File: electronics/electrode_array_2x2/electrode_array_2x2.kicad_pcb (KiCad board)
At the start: 2 copper layers, 2 parts

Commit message: WIP PCB layout
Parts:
- added J1: Conn_01x04, Connector_JST:JST_PH_B4B-PH-SM4-TB_1x04-1MP_P2.00mm_Vertical, F.Cu at (150.0, 105.0)
- added J2: Electrode_A1, SquantorSpecial:hugepad_50X15hole, F.Cu at (145.0, 100.0)
- added J3: Electrode_B1, SquantorSpecial:hugepad_50X15hole, F.Cu at (155.0, 100.0)
- added J4: Electrode_A2, SquantorSpecial:hugepad_50X15hole, F.Cu at (145.0, 110.0)
- added J5: Electrode_B2, SquantorSpecial:hugepad_50X15hole, F.Cu at (155.0, 110.0)
- N2: value 20190704 -> 20191222
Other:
- board outline added: 20 x 20 mm
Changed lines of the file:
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@@
-(kicad_pcb (version 20171130) (host pcbnew 5.1.2-f72e74a~84~ubuntu18.04.1)
+(kicad_pcb (version 20171130) (host pcbnew 5.1.5-52549c5~84~ubuntu18.04.1)
   (general
     (thickness 1.6)
-    (drawings 0)
+    (drawings 4)
     (tracks 0)
     (zones 0)
-    (modules 2)
-    (nets 1)
+    (modules 7)
+    (nets 5)
   )
   (page A4)
@@
   )
   (net 0 "")
+  (net 1 /Electrode_B2)
+  (net 2 /Electrode_A2)
+  (net 3 /Electrode_B1)
+  (net 4 /Electrode_A1)
   (net_class Default "This is the default net class."
     (clearance 0.1524)
@@
     (uvia_dia 0.381)
     (uvia_drill 0.254)
+    (add_net /Electrode_A1)
+    (add_net /Electrode_A2)
+    (add_net /Electrode_B1)
+    (add_net /Electrode_B2)
+  )
+  (module Connector_JST:JST_PH_B4B-PH-SM4-TB_1x04-1MP_P2.00mm_Vertical (layer F.Cu)
+    (at 150 105)
+    (descr "JST PH series connector, B4B-PH-SM4-TB (http://www.jst-mfg.com/product/pdf/eng/ePH.pdf), generated with kicad-footprint-generator")
+    (tags "connector JST PH side entry")
+    (attr smd)
+    (fp_text reference J1 (at 0 -5.45) (layer F.SilkS)
+      (effects (font (size 1 1) (thickness 0.15)))
+    )
+    (fp_text value Conn_01x04 (at 0 4.45) (layer F.Fab)
+      (effects (font (size 1 1) (thickness 0.15)))
+    )
+    (fp_text user %R (at 0 -1) (layer F.Fab)
+      (effects (font (size 1 1) (thickness 0.15)))
+    )
+    (fp_line (start -3 0.042893) (end -2.5 0.75) (layer F.Fab) (width 0.1))
+    (fp_line (start -3.5 0.75) (end -3 0.042893) (layer F.Fab) (width 0.1))
+    (fp_line (start 6.7 -4.75) (end -6.7 -4.75) (layer F.CrtYd) (width 0.05))
+    (fp_line (start 6.7 3.75) (end 6.7 -4.75) (layer F.CrtYd) (width 0.05))
+    (fp_line (start -6.7 3.75) (end 6.7 3.75) (layer F.CrtYd) (width 0.05))
+    (fp_line (start -6.7 -4.75) (end -6.7 3.75) (layer F.CrtYd) (width 0.05))
+    (fp_line (start 3.25 -2.75) (end 2.75 -2.75) (layer F.Fab) (width 0.1))
+    (fp_line (start 3.25 -2.25) (end 3.25 -2.75) (layer F.Fab) (width 0.1))
+    (fp_line (start 2.75 -2.25) (end 3.25 -2.25) (layer F.Fab) (width 0.1))
+    (fp_line (start 2.75 -2.75) (end 2.75 -2.25) (layer F.Fab) (width 0.1))
+    (fp_line (start 1.25 -2.75) (end 0.75 -2.75) (layer F.Fab) (width 0.1))
+    (fp_line (start 1.25 -2.25) (end 1.25 -2.75) (layer F.Fab) (width 0.1))
+    (fp_line (start 0.75 -2.25) (end 1.25 -2.25) (layer F.Fab) (width 0.1))
+    (fp_line (start 0.75 -2.75) (end 0.75 -2.25) (layer F.Fab) (width 0.1))
+    (fp_line (start -0.75 -2.75) (end -1.25 -2.75) (layer F.Fab) (width 0.1))
+    (fp_line (start -0.75 -2.25) (end -0.75 -2.75) (layer F.Fab) (width 0.1))
+    (fp_line (start -1.25 -2.25) (end -0.75 -2.25) (layer F.Fab) (width 0.1))
+    (fp_line (start -1.25 -2.75) (end -1.25 -2.25) (layer F.Fab) (width 0.1))
+    (fp_line (start -2.75 -2.75) (end -3.25 -2.75) (layer F.Fab) (width 0.1))
+    (fp_line (start -2.75 -2.25) (end -2.75 -2.75) (layer F.Fab) (width 0.1))
+    (fp_line (start -3.25 -2.25) (end -2.75 -2.25) (layer F.Fab) (width 0.1))
+    (fp_line (start -3.25 -2.75) (end -3.25 -2.25) (layer F.Fab) (width 0.1))
+    (fp_line (start 5.975 0.75) (end 5.975 -4.25) (layer F.Fab) (width 0.1))
+    (fp_line (start -5.975 0.75) (end -5.975 -4.25) (layer F.Fab) (width 0.1))
+    (fp_line (start -5.975 -4.25) (end 5.975 -4.25) (layer F.Fab) (width 0.1))
+    (fp_line (start 6.085 -4.36) (end 6.085 -3.51) (layer F.SilkS) (width 0.12))
+    (fp_line (start -6.085 -4.36) (end 6.085 -4.36) (layer F.SilkS) (width 0.12))
+    (fp_line (start -6.085 -3.51) (end -6.085 -4.36) (layer F.SilkS) (width 0.12))
+    (fp_line (start 6.085 0.86) (end 3.76 0.86) (layer F.SilkS) (width 0.12))
+    (fp_line (start 6.085 0.01) (end 6.085 0.86) (layer F.SilkS) (width 0.12))
+    (fp_line (start -3.76 0.86) (end -3.76 3.25) (layer F.SilkS) (width 0.12))
+    (fp_line (start -6.085 0.86) (end -3.76 0.86) (layer F.SilkS) (width 0.12))
+    (fp_line (start -6.085 0.01) (end -6.085 0.86) (layer F.SilkS) (width 0.12))
+    (fp_line (start -5.975 0.75) (end 5.975 0.75) (layer F.Fab) (width 0.1))
+    (pad MP smd roundrect (at 5.4 -1.75) (size 1.6 3) (layers F.Cu F.Paste F.Mask) (roundrect_rratio 0.15625))
+    (pad MP smd roundrect (at -5.4 -1.75) (size 1.6 3) (layers F.Cu F.Paste F.Mask) (roundrect_rratio 0.15625))
+    (pad 4 smd roundrect (at 3 0.5) (size 1 5.5) (layers F.Cu F.Paste F.Mask) (roundrect_rratio 0.25)
+      (net 1 /Electrode_B2))
+    (pad 3 smd roundrect (at 1 0.5) (size 1 5.5) (layers F.Cu F.Paste F.Mask) (roundrect_rratio 0.25)
+      (net 2 /Electrode_A2))
+    (pad 2 smd roundrect (at -1 0.5) (size 1 5.5) (layers F.Cu F.Paste F.Mask) (roundrect_rratio 0.25)
+      (net 3 /Electrode_B1))
+    (pad 1 smd roundrect (at -3 0.5) (size 1 5.5) (layers F.Cu F.Paste F.Mask) (roundrect_rratio 0.25)
+      (net 4 /Electrode_A1))
+    (model ${KISYS3DMOD}/Connector_JST.3dshapes/JST_PH_B4B-PH-SM4-TB_1x04-1MP_P2.00mm_Vertical.wrl
+      (at (xyz 0 0 0))
+      (scale (xyz 1 1 1))
+      (rotate (xyz 0 0 0))
+    )
+  )
+  (module SquantorSpecial:hugepad_50X15hole (layer F.Cu)
+    (at 155 110)
+    (fp_text reference J5 (at 0 -4) (layer F.SilkS)
+      (effects (font (size 1 1) (thickness 0.15)))
+    )
+    (fp_text value Electrode_B2 (at 0 4) (layer F.Fab)
+      (effects (font (size 1 1) (thickness 0.15)))
+    )
+    (pad 1 thru_hole circle (at 0 0) (size 5 5) (drill 1.5) (layers *.Cu *.Mask)
+      (net 1 /Electrode_B2))
+  )
+  (module SquantorSpecial:hugepad_50X15hole (layer F.Cu)
+    (at 145 110)
+    (fp_text reference J4 (at 0 -4) (layer F.SilkS)
+      (effects (font (size 1 1) (thickness 0.15)))
+    )
+    (fp_text value Electrode_A2 (at 0 4) (layer F.Fab)
+      (effects (font (size 1 1) (thickness 0.15)))
+    )
+    (pad 1 thru_hole circle (at 0 0) (size 5 5) (drill 1.5) (layers *.Cu *.Mask)
+      (net 2 /Electrode_A2))
+  )
+  (module SquantorSpecial:hugepad_50X15hole (layer F.Cu)
+    (at 155 100)
+    (fp_text reference J3 (at 0 -4) (layer F.SilkS)
+      (effects (font (size 1 1) (thickness 0.15)))
+    )
+    (fp_text value Electrode_B1 (at 0 4) (layer F.Fab)
+      (effects (font (size 1 1) (thickness 0.15)))
+    )
+    (pad 1 thru_hole circle (at 0 0) (size 5 5) (drill 1.5) (layers *.Cu *.Mask)
+      (net 3 /Electrode_B1))
+  )
+  (module SquantorSpecial:hugepad_50X15hole (layer F.Cu)
+    (at 145 100)
+    (fp_text reference J2 (at 0 -4) (layer F.SilkS)
+      (effects (font (size 1 1) (thickness 0.15)))
+    )
+    (fp_text value Electrode_A1 (at 0 4) (layer F.Fab)
+      (effects (font (size 1 1) (thickness 0.15)))
+    )
+    (pad 1 thru_hole circle (at 0 0) (size 5 5) (drill 1.5) (layers *.Cu *.Mask)
+      (net 4 /Electrode_A1))
   )
   (module Symbols:OSHW-Symbol_6.7x6mm_SilkScreen (layer F.Cu)
@@
       (effects (font (size 1 1) (thickness 0.15)))
     )
-    (fp_text value 20190704 (at -0.4 -0.1) (layer F.SilkS)
+    (fp_text value 20191222 (at -0.4 -0.1) (layer F.SilkS)
       (effects (font (size 1 1) (thickness 0.15)))
     )
@@
     )
   )
+  (gr_line (start 140 115) (end 140 95) (layer Edge.Cuts) (width 0.15))
+  (gr_line (start 160 115) (end 140 115) (layer Edge.Cuts) (width 0.15))
+  (gr_line (start 160 95) (end 160 115) (layer Edge.Cuts) (width 0.15))
+  (gr_line (start 140 95) (end 160 95) (layer Edge.Cuts) (width 0.15))
 )

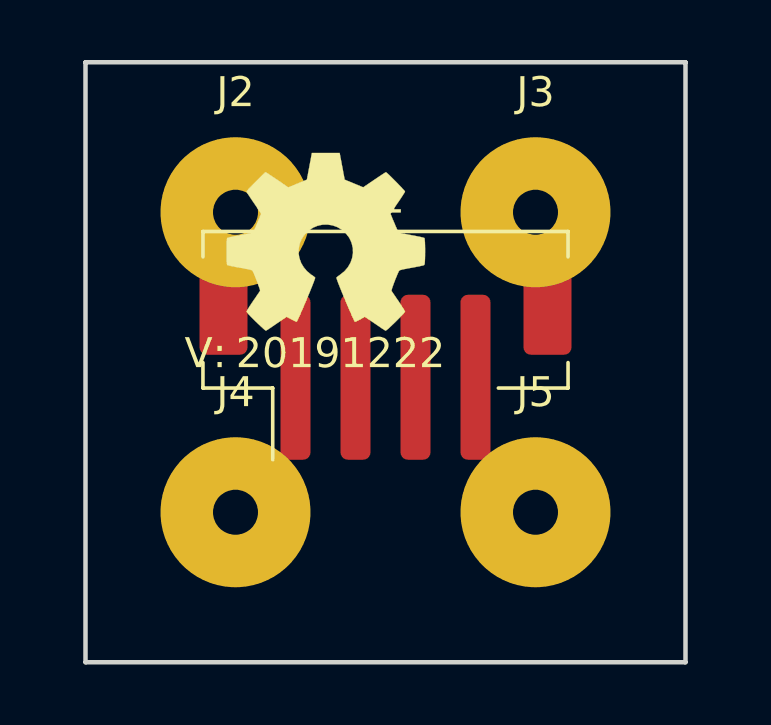
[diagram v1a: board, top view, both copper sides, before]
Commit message: changed connector, silk placement
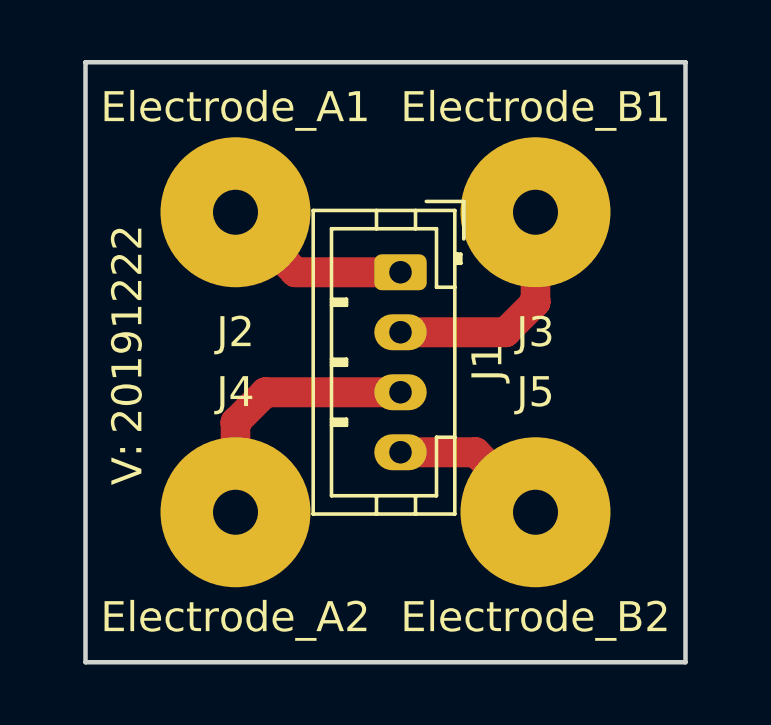
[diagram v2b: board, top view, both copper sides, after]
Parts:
- removed N1: OHWLOGO, Symbols:OSHW-Symbol_6.7x6mm_SilkScreen
- J1: footprint Connector_JST:JST_PH_B4B-PH-SM4-TB_1x04-1MP_P2.00mm_Vertical -> Connector_JST:JST_PH_B4B-PH-K_1x04_P2.00mm_Vertical
- moved N2 7.51 mm to (141.5, 103.5), turned to 90 degrees
- moved J1 3.04 mm to (150.5, 102.0), turned to 270 degrees
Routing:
- net /Electrode_A2: track 0.00 -> 8.91 mm
- net /Electrode_B1: track 0.00 -> 7.91 mm
- net /Electrode_A1: track 0.00 -> 6.33 mm
- net /Electrode_B2: track 0.00 -> 5.33 mm

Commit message: updated electrode array pcb to larger hole sizes
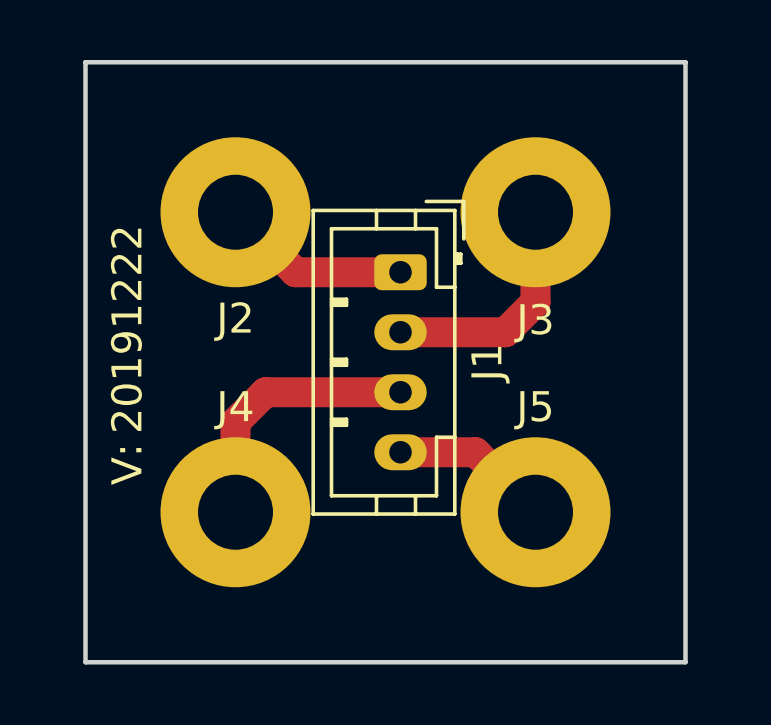
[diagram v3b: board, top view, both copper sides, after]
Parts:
- J2, J3, J4, J5: footprint SquantorSpecial:hugepad_50X15hole -> SquantorSpecial:hugepad_50X25hole
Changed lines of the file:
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@@
-(kicad_pcb (version 20171130) (host pcbnew 5.1.5-52549c5~84~ubuntu18.04.1)
+(kicad_pcb (version 20171130) (host pcbnew 5.1.5-52549c5~86~ubuntu19.10.1)
   (general
     (thickness 1.6)
@@
   )
   (setup
-    (last_trace_width 1)
+    (last_trace_width 0.1524)
     (user_trace_width 0.1524)
     (user_trace_width 0.2)
@@
     (add_net /Electrode_B2)
   )
+  (module SquantorSpecial:hugepad_50X25hole (layer F.Cu)
+    (at 155 110)
+    (fp_text reference J5 (at 0 -3.5) (layer F.SilkS)
+      (effects (font (size 1 1) (thickness 0.15)))
+    )
+    (fp_text value Electrode_B2 (at 0 3.5) (layer F.Fab)
+      (effects (font (size 1 1) (thickness 0.15)))
+    )
+    (pad 1 thru_hole circle (at 0 0) (size 5 5) (drill 2.5) (layers *.Cu *.Mask)
+      (net 1 /Electrode_B2))
+  )
+  (module SquantorSpecial:hugepad_50X25hole (layer F.Cu)
+    (at 145 110)
+    (fp_text reference J4 (at 0 -3.5) (layer F.SilkS)
+      (effects (font (size 1 1) (thickness 0.15)))
+    )
+    (fp_text value Electrode_A2 (at 0 3.5) (layer F.Fab)
+      (effects (font (size 1 1) (thickness 0.15)))
+    )
+    (pad 1 thru_hole circle (at 0 0) (size 5 5) (drill 2.5) (layers *.Cu *.Mask)
+      (net 2 /Electrode_A2))
+  )
+  (module SquantorSpecial:hugepad_50X25hole (layer F.Cu)
+    (at 155 100)
+    (fp_text reference J3 (at 0 3.6) (layer F.SilkS)
+      (effects (font (size 1 1) (thickness 0.15)))
+    )
+    (fp_text value Electrode_B1 (at 0 3.5) (layer F.Fab)
+      (effects (font (size 1 1) (thickness 0.15)))
+    )
+    (pad 1 thru_hole circle (at 0 0) (size 5 5) (drill 2.5) (layers *.Cu *.Mask)
+      (net 3 /Electrode_B1))
+  )
+  (module SquantorSpecial:hugepad_50X25hole (layer F.Cu)
+    (at 145 100)
+    (fp_text reference J2 (at 0 3.55) (layer F.SilkS)
+      (effects (font (size 1 1) (thickness 0.15)))
+    )
+    (fp_text value Electrode_A1 (at 0 3.5) (layer F.Fab)
+      (effects (font (size 1 1) (thickness 0.15)))
+    )
+    (pad 1 thru_hole circle (at 0 0) (size 5 5) (drill 2.5) (layers *.Cu *.Mask)
+      (net 4 /Electrode_A1))
+  )
   (module Connector_JST:JST_PH_B4B-PH-K_1x04_P2.00mm_Vertical (layer F.Cu)
     (at 150.5 102 270)
@@
     )
   )
-  (module SquantorSpecial:hugepad_50X15hole (layer F.Cu)
-    (at 155 110)
-    (fp_text reference J5 (at 0 -4) (layer F.SilkS)
-      (effects (font (size 1 1) (thickness 0.15)))
-    )
-    (fp_text value Electrode_B2 (at 0 3.5) (layer F.SilkS)
-      (effects (font (size 1 1) (thickness 0.15)))
-    )
-    (pad 1 thru_hole circle (at 0 0) (size 5 5) (drill 1.5) (layers *.Cu *.Mask)
-      (net 1 /Electrode_B2))
-  )
-  (module SquantorSpecial:hugepad_50X15hole (layer F.Cu)
-    (at 145 110)
-    (fp_text reference J4 (at 0 -4) (layer F.SilkS)
-      (effects (font (size 1 1) (thickness 0.15)))
-    )
-    (fp_text value Electrode_A2 (at 0 3.5) (layer F.SilkS)
-      (effects (font (size 1 1) (thickness 0.15)))
-    )
-    (pad 1 thru_hole circle (at 0 0) (size 5 5) (drill 1.5) (layers *.Cu *.Mask)
-      (net 2 /Electrode_A2))
-  )
-  (module SquantorSpecial:hugepad_50X15hole (layer F.Cu)
-    (at 155 100)
-    (fp_text reference J3 (at 0 4) (layer F.SilkS)
-      (effects (font (size 1 1) (thickness 0.15)))
-    )
-    (fp_text value Electrode_B1 (at 0 -3.5) (layer F.SilkS)
-      (effects (font (size 1 1) (thickness 0.15)))
-    )
-    (pad 1 thru_hole circle (at 0 0) (size 5 5) (drill 1.5) (layers *.Cu *.Mask)
-      (net 3 /Electrode_B1))
-  )
-  (module SquantorSpecial:hugepad_50X15hole (layer F.Cu)
-    (at 145 100)
-    (fp_text reference J2 (at 0 4) (layer F.SilkS)
-      (effects (font (size 1 1) (thickness 0.15)))
-    )
-    (fp_text value Electrode_A1 (at 0 -3.5) (layer F.SilkS)
-      (effects (font (size 1 1) (thickness 0.15)))
-    )
-    (pad 1 thru_hole circle (at 0 0) (size 5 5) (drill 1.5) (layers *.Cu *.Mask)
-      (net 4 /Electrode_A1))
-  )
   (module SquantorLabels:Label_version (layer F.Cu)
